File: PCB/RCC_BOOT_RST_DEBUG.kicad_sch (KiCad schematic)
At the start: 21 parts, among them U2 STM32MP157FABx, Y1 ECS-2520MVQ-240

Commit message: Look like MPU done
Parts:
- removed R35, R36: 0, symbol Device:R
- added J2: FTSH-107-01-L-DV-K-A, FTSH-107-01-L-DV-K-A:SAMTEC_FTSH-107-01-L-DV-K-A, symbol FTSH-107-01-L-DV-K-A:FTSH-107-01-L-DV-K-A
- added JP1, JP2, JP3: SolderJumper_3_Bridged12, Jumper:SolderJumper-3_P1.3mm_Bridged12_Pad1.0x1.5mm, symbol Jumper:SolderJumper_3_Bridged12
- added R41: 10k, symbol Device:R
- added R42: 100, symbol Device:R
- added TP10, TP11, TP12, TP13, TP6, TP7, TP8, TP9: TestPoint, TestPoint:TestPoint_Pad_D1.0mm, symbol Connector:TestPoint
- added U6, U7: HSP051-4M10, HSP051-4M10:IC_HSP051-4M10, symbol HSP051-4M10:HSP051-4M10
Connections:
- net GND: now also C95.1, D1.A, S2.1, S2.2, J2.05, J2.07, JP2.3 (B), JP3.3 (B), R42.1, U6.3 (GND), U6.8 (GND), U7.3 (GND), U7.8 (GND)
- net NRST: now also C95.2, D1.C, S2.3, S2.4, J2.12, R41.1, TP10.1, U7.1 (I/O_1), U7.10 (NC)
- net VDD: now also J2.03, JP2.1 (A), JP3.1 (A), R41.2, U7.5 (I/O_4), U7.6 (NC)
- net T_JTDI/NC: now reaches U2.D13 (JTDI)
- net T_JTDI/NC: now also J2.10, TP9.1, U6.5 (I/O_4), U6.6 (NC)
- net T_JTDO/T_SWO: now reaches U2.D14 (JTDO)
- net T_JTDO/T_SWO: now also J2.08, TP8.1, U6.4 (I/O_3), U6.7 (NC)
- net T_JTMS/T_SWDIO: now reaches U2.D15 (JTMS)
- net T_JTMS/T_SWDIO: now also J2.04, TP6.1, U6.1 (I/O_1), U6.10 (NC)
- net T_JCLK/T_SWCLK: now reaches U2.D16 (JTCK)
- net T_JCLK/T_SWCLK: now also J2.06, TP7.1, U6.2 (I/O_2), U6.9 (NC)
- net at U2.N1 (PDR_ON_CORE): now also JP3.2 (C)
- net at U2.N2 (PDR_ON): now also JP2.2 (C)
- net at U2.T15 (BYPASS_REG1V8): now also JP1.2 (C)
- new net: J2.11, R42.2, TP13.1
- new net T_VCP_RX: J2.13, TP12.1, U7.4 (I/O_3), U7.7 (NC)
- new net T_VCP_TX: J2.14, TP11.1, U7.2 (I/O_2), U7.9 (NC)
- no-connect marks 0 -> 4
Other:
- moved on the sheet: C91, C92, C93, C94, C95, D1, R31, R32, R33, R34, R37, R38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

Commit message: PCB_UPDATE
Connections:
- net T_VCP_RX renamed UART4_TX_STM
- net T_VCP_TX renamed UART4_RX_STM
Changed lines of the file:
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@@
-	(wire
-		(pts
-			(xy 264.16 127) (xy 316.23 127)
-		)
-		(stroke
-			(width 0)
-			(type default)
-		)
-	)
 	(wire
 		(pts
@@
 	(wire
 		(pts
+			(xy 254 127) (xy 316.23 127)
+		)
+		(stroke
+			(width 0)
+			(type default)
+		)
+	)
+	(wire
+		(pts
 			(xy 265.43 74.93) (xy 265.43 73.66)
 		)
@@
 	(wire
 		(pts
-			(xy 264.16 132.08) (xy 321.31 132.08)
-		)
-		(stroke
-			(width 0)
-			(type default)
-		)
-	)
-	(wire
-		(pts
 			(xy 290.83 52.07) (xy 297.18 52.07)
 		)
@@
 		(pts
 			(xy 283.21 33.02) (xy 280.67 33.02)
+		)
+		(stroke
+			(width 0)
+			(type default)
+		)
+	)
+	(wire
+		(pts
+			(xy 254 132.08) (xy 321.31 132.08)
 		)
 		(stroke
@@
 			)
 			(justify right bottom)
+		)
+	)
+	(global_label "UART4_TX_STM"
+		(shape input)
+		(at 254 132.08 180)
+		(fields_autoplaced yes)
+		(effects
+			(font
+				(size 1.27 1.27)
+			)
+			(justify right)
+		)
+		(property "Intersheetrefs" "${INTERSHEET_REFS}"
+			(at 237.4078 132.08 0)
+			(effects
+				(font
+					(size 1.27 1.27)
+				)
+				(justify right)
+				(hide yes)
+			)
 		)
 	)
@@
 			(effects
 				(font
+					(size 1.27 1.27)
+				)
+				(justify right)
+				(hide yes)
+			)
+		)
+	)
+	(global_label "UART4_RX_STM"
+		(shape input)
+		(at 254 127 180)
+		(fields_autoplaced yes)
+		(effects
+			(font
+				(size 1.27 1.27)
+			)
+			(justify right)
+		)
+		(property "Intersheetrefs" "${INTERSHEET_REFS}"
+			(at 237.1054 127 0)
+			(effects
+				(font

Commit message: PCB_UPDATE
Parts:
- R31, R32, R33, R34, R37, R38, R39, R41, R42: footprint (none) -> Resistor_SMD:R_0402_1005Metric
- S1: footprint DS04-254-2-03BK-SMT:SW_DS04-254-2-03BK-SMT -> lib:SW_DS04-254-2-03BK-SMT
- S2: footprint PTS525SM15SMTR2LFS:SW_PTS525SM15SMTR2LFS -> lib:SW_PTS525SM15SMTR2LFS
- U6, U7: footprint HSP051-4M10:IC_HSP051-4M10 -> lib:IC_HSP051-4M10
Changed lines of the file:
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@@
 			)
 		)
-		(property "Footprint" ""
+		(property "Footprint" "Resistor_SMD:R_0402_1005Metric"
 			(at 257.81 75.438 90)
 			(effects
@@
 			)
 		)
-		(property "Footprint" "HSP051-4M10:IC_HSP051-4M10"
+		(property "Footprint" "lib:IC_HSP051-4M10"
 			(at 260.35 162.56 0)
 			(effects
@@
 			)
 		)
-		(property "Footprint" ""
+		(property "Footprint" "Resistor_SMD:R_0402_1005Metric"
 			(at 70.358 31.75 90)
 			(effects
@@
 			)
 		)
-		(property "Footprint" ""
+		(property "Footprint" "Resistor_SMD:R_0402_1005Metric"
 			(at 155.702 86.36 90)
 			(effects
@@
 			)
 		)
-		(property "Footprint" "DS04-254-2-03BK-SMT:SW_DS04-254-2-03BK-SMT"
+		(property "Footprint" "lib:SW_DS04-254-2-03BK-SMT"
 			(at 133.35 73.66 0)
 			(effects
@@
 			)
 		)
-		(property "Footprint" ""
+		(property "Footprint" "Resistor_SMD:R_0402_1005Metric"
 			(at 251.968 63.5 90)
 			(effects
@@
 			)
 		)
-		(property "Footprint" ""
+		(property "Footprint" "Resistor_SMD:R_0402_1005Metric"
 			(at 168.148 86.36 90)
 			(effects
@@
 			)
 		)
-		(property "Footprint" "PTS525SM15SMTR2LFS:SW_PTS525SM15SMTR2LFS"
+		(property "Footprint" "lib:SW_PTS525SM15SMTR2LFS"
 			(at 66.04 48.26 0)
 			(effects
@@
 			)
 		)
-		(property "Footprint" "HSP051-4M10:IC_HSP051-4M10"
+		(property "Footprint" "lib:IC_HSP051-4M10"
 			(at 302.26 162.56 0)
 			(effects
@@
 			)
 		)
-		(property "Footprint" ""
+		(property "Footprint" "Resistor_SMD:R_0402_1005Metric"
 			(at 243.84 53.848 90)
 			(effects
@@
 			)
 		)
-		(property "Footprint" ""
+		(property "Footprint" "Resistor_SMD:R_0402_1005Metric"
 			(at 282.448 38.1 90)
 			(effects
@@
 			)
 		)
-		(property "Footprint" ""
+		(property "Footprint" "Resistor_SMD:R_0402_1005Metric"
 			(at 150.368 86.36 90)
 			(effects
@@
 			)
 		)
-		(property "Footprint" ""
+		(property "Footprint" "Resistor_SMD:R_0402_1005Metric"
 			(at 379.222 129.54 90)
 			(effects
@@
 					(reference "U2")
 					(unit 5)
+				)
+				(path "/65890f61-d586-475b-928a-b635a5e4e59e/9899e005-10ba-4bf4-b936-8d0d8a1813b9"
+					(reference "U2")
+					(unit 5)

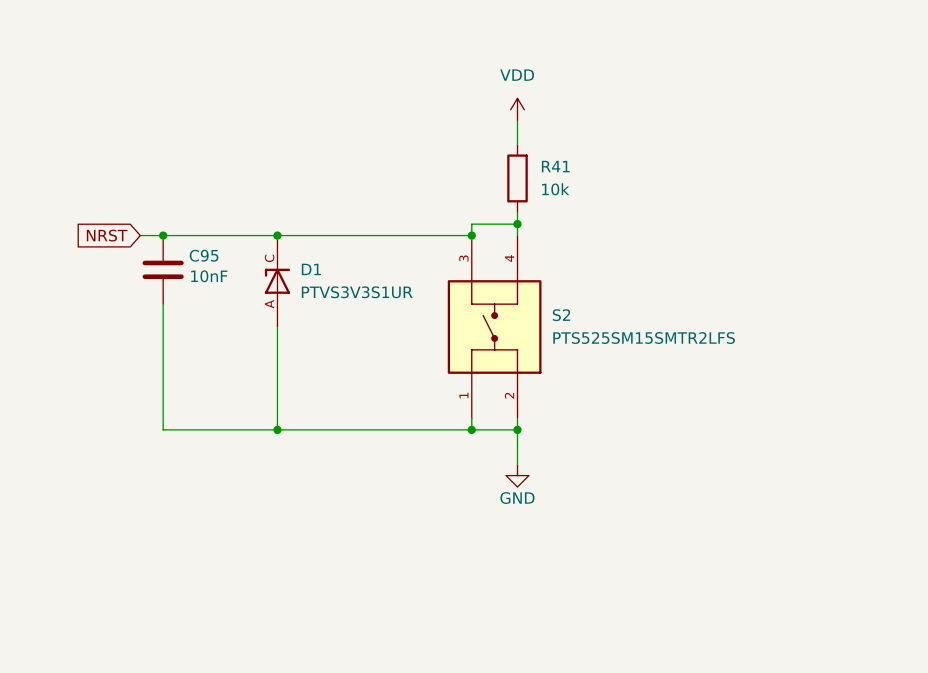
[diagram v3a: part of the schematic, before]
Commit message: added eMMC
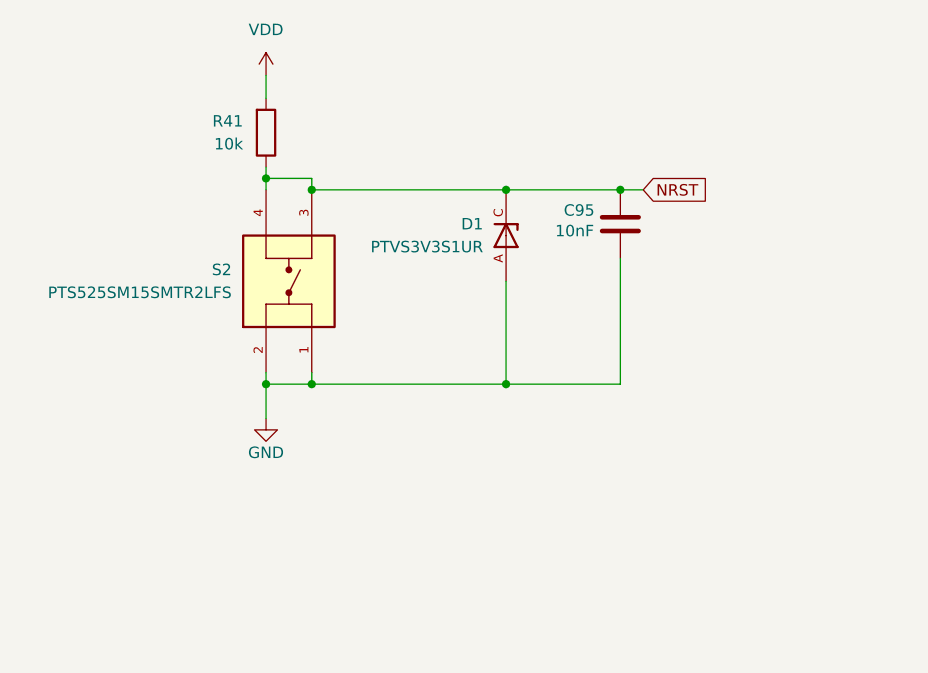
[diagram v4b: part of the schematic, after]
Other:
- moved on the sheet: C95, D1, R41, S2

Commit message: wifi done
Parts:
- removed JP1, JP2, JP3: SolderJumper_3_Bridged12, Jumper:SolderJumper-3_P1.3mm_Bridged12_Pad1.0x1.5mm, symbol Jumper:SolderJumper_3_Bridged12
- added R84, R85, R86, R87, R88, R89: 0, Resistor_SMD:R_0402_1005Metric, symbol Device:R
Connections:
- net GND: now also R85.1, R87.1, R89.1
- net VDD: now also R84.2, R86.2, R88.2
- net at U2.N2 (PDR_ON): now also R86.1, R87.2
- net at U2.N1 (PDR_ON_CORE): now also R84.1, R85.2

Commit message: PCB_UPDATE
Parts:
- removed S2: PTS525SM15SMTR2LFS, lib:SW_PTS525SM15SMTR2LFS, symbol PTS525SM15SMTR2LFS:PTS525SM15SMTR2LFS
- added S701: EVQ-9P701P, lib:SW_EVQ-9P701P, symbol EVQ-9P701P:EVQ-9P701P
- D701: renamed from D1; footprint PTVS3V3S1UR:TVS_PTVS3V3S1UR -> lib:TVS_PTVS3V3S1UR
- J701: renamed from J2; footprint FTSH-107-01-L-DV-K-A:SAMTEC_FTSH-107-01-L-DV-K-A -> lib:SAMTEC_FTSH-107-01-L-DV-K-A
- renumbered C95 to C701, C94 to C702, C92 to C703, C91 to C704, C93 to C705, R41 to R701, R88 to R702, R89 to R703, R84 to R704, R85 to R705, R39 to R706, R86 to R707, R87 to R708, R37 to R709, R38 to R710, R32 to R711, R33 to R712, R34 to R713, R31 to R714, R42 to R715, S1 to S702, TP5 to TP701, TP4 to TP702, TP6 to TP703, TP7 to TP704, TP8 to TP705, TP9 to TP706, TP10 to TP707, TP11 to TP708, TP12 to TP709, TP13 to TP710, U2 to U301, U6 to U701, U7 to U702, Y1 to Y701
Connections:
- net GND: now also S701.2A, S701.2B, S701.2C, S701.2D
- net NRST: now also S701.1A, S701.1B

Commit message: PCB_UPDATE
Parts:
- TP701, TP702, TP703, TP704, TP705, TP706, TP707, TP708, TP709, TP710: footprint TestPoint:TestPoint_Pad_D1.0mm -> Library:TP_0.5mm
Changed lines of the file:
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@@
 		)
 	)
+	(rule_area
+		(polyline
+			(pts
+				(xy 407.67 12.7) (xy 407.67 251.46) (xy 298.45 251.46) (xy 298.45 283.21) (xy 297.18 284.48) (xy 12.7 284.48)
+				(xy 12.7 12.7)
+			)
+			(stroke
+				(width 0)
+				(type dash)
+			)
+			(fill
+				(type none)
+			)
+		)
+	)
+	(netclass_flag ""
+		(length 2.54)
+		(shape round)
+		(at 59.69 12.7 180)
+		(fields_autoplaced yes)
+		(effects
+			(font
+				(size 1.27 1.27)
+			)
+			(justify right bottom)
+		)
+		(property "Netclass" "RCC_BOOT_RST_DEBUG"
+			(at 60.3885 15.24 0)
+			(effects
+				(font
+					(size 1.27 1.27)
+				)
+				(justify left)
+			)
+		)
+		(property "Component Class" ""
+			(at -128.27 1.27 0)
+			(effects
+				(font
+					(size 1.27 1.27)
+					(italic yes)
+				)
+			)
+		)
+	)
 	(symbol
 		(lib_id "Connector:TestPoint")
@@
 			)
 		)
-		(property "Footprint" "TestPoint:TestPoint_Pad_D1.0mm"
+		(property "Footprint" "Library:TP_0.5mm"
 			(at 321.31 107.95 0)
 			(effects
@@
 			)
 		)
-		(property "Footprint" "TestPoint:TestPoint_Pad_D1.0mm"
+		(property "Footprint" "Library:TP_0.5mm"
 			(at 144.78 115.57 0)
 			(effects
@@
 			)
 		)
-		(property "Footprint" "TestPoint:TestPoint_Pad_D1.0mm"
+		(property "Footprint" "Library:TP_0.5mm"
 			(at 328.93 107.95 0)
 			(effects
@@
 			)
 		)
-		(property "Footprint" "TestPoint:TestPoint_Pad_D1.0mm"
+		(property "Footprint" "Library:TP_0.5mm"
 			(at 313.69 107.95 0)
 			(effects
@@
 			)
 		)
-		(property "Footprint" "TestPoint:TestPoint_Pad_D1.0mm"
+		(property "Footprint" "Library:TP_0.5mm"
 			(at 294.64 107.95 0)
 			(effects
@@
 			)
 		)
-		(property "Footprint" "TestPoint:TestPoint_Pad_D1.0mm"
+		(property "Footprint" "Library:TP_0.5mm"
 			(at 300.99 107.95 0)
 			(effects
@@
 			)
 		)
-		(property "Footprint" "TestPoint:TestPoint_Pad_D1.0mm"
+		(property "Footprint" "Library:TP_0.5mm"
 			(at 307.34 107.95 0)
 			(effects
@@
 			)
 		)
-		(property "Footprint" "TestPoint:TestPoint_Pad_D1.0mm"
+		(property "Footprint" "Library:TP_0.5mm"
 			(at 375.92 109.22 0)
 			(effects
@@
 			)
 		)
-		(property "Footprint" "TestPoint:TestPoint_Pad_D1.0mm"
+		(property "Footprint" "Library:TP_0.5mm"
 			(at 151.13 115.57 0)
 			(effects
@@
 			)
 		)
-		(property "Footprint" "TestPoint:TestPoint_Pad_D1.0mm"
+		(property "Footprint" "Library:TP_0.5mm"
 			(at 288.29 107.95 0)
 			(effects
